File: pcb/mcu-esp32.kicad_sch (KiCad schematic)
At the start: 13 parts, among them Q4 BSS138, Q5 BSS138, U10 ESP32-S3-WROOM-1-N8R8

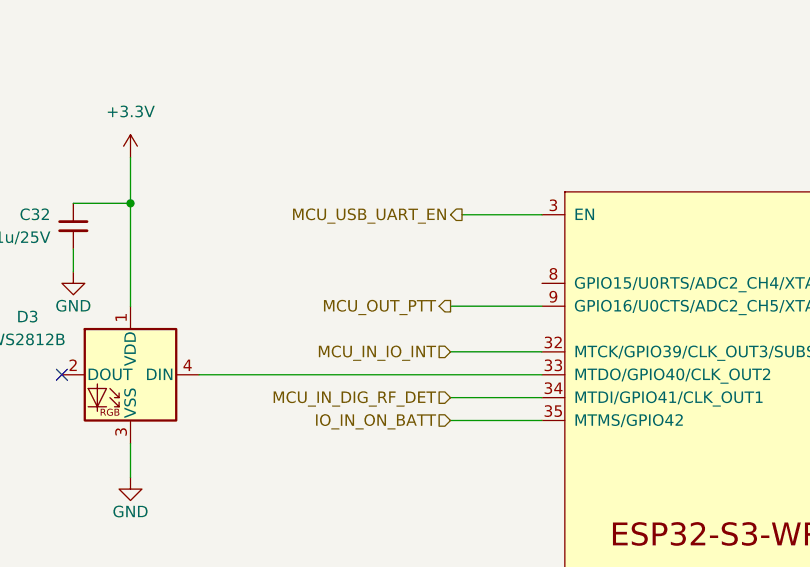
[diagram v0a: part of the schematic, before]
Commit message: Move audio jack (J6) into SA818V sheet, rename nets/jumpers for clarity
Relocates the switched TRS jack from audio.kicad_sch into SA818V.kicad_sch
and updates the root sheet's pin interface to match (SA818_IN_MIC,
SA818_IN_PTT, new SA818_IN_PTT_HB), fixing an I2C_MIC_OUT/I2S_MIC_OUT
naming typo along the way. Ring/ring-switch/sleeve are wired; tip and
tip-switch (mic audio leg) are still open, per audio_ptt_path.md.

Also: renames GPS hierarchical labels and several power/regulation/
peripheral jumper values from generic (Jumper_2_Open, SolderJumper_2_Open)
to descriptive names, wires MCU_OUT_PTT_HB, and removes now-unused test
points/jumpers from the battery input sheets. Adds 74hc123_pinout.md
planning doc for the TX-safety timeout / force-off failsafe part.

Co-Authored-By: Claude Sonnet 5 <noreply@anthropic.com>
Claude-Session: https://claude.ai/code/session_01P3G1ionr2QCR8SZtKRreL3
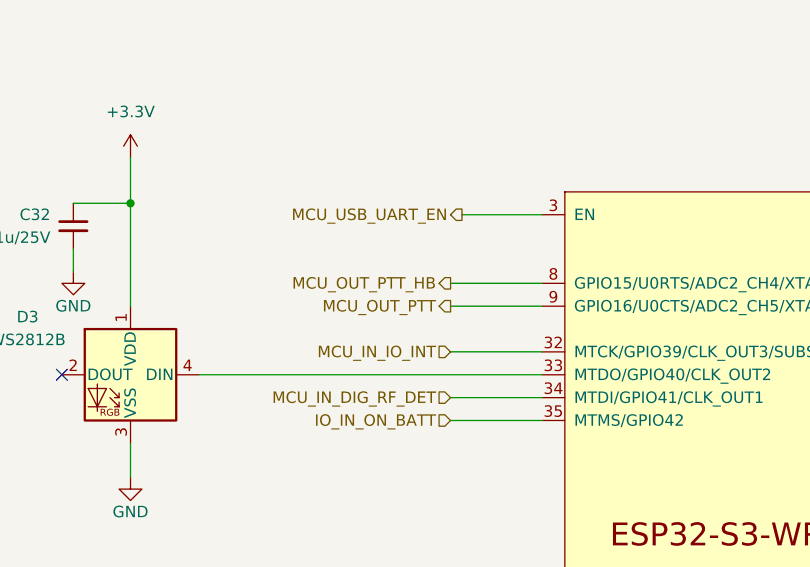
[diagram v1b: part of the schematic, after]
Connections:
- net MCU_OUT_PTT_HB: now reaches U10.8 (GPIO15/U0RTS/ADC2_CH4/XTAL_32K_P)
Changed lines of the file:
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@@
+	(wire
+		(pts
+			(xy 68.58 62.23) (xy 78.74 62.23)
+		)
+		(stroke
+			(width 0)
+			(type default)
+		)
+	)
 	(wire
 		(pts
@@
 		)
 	)
+	(hierarchical_label "MCU_OUT_PTT_HB"
+		(shape output)
+		(at 68.58 62.23 180)
+		(effects
+			(font
+				(size 1.27 1.27)
+			)
+			(justify right)
+		)
+	)
